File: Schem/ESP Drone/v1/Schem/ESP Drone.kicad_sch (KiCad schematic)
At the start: 80 parts, among them J1 Micro_SD_Card, J2 GEPRC M10 FPV, J3 Conn_01x03_Pin, J4 Conn_01x03_Pin, J5 Conn_01x03_Pin, J6 Conn_01x03_Pin, J7 Conn_Coaxial, U1 ESP32-S2-WROVER, U2 TPS563200, U3 MPU-6050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

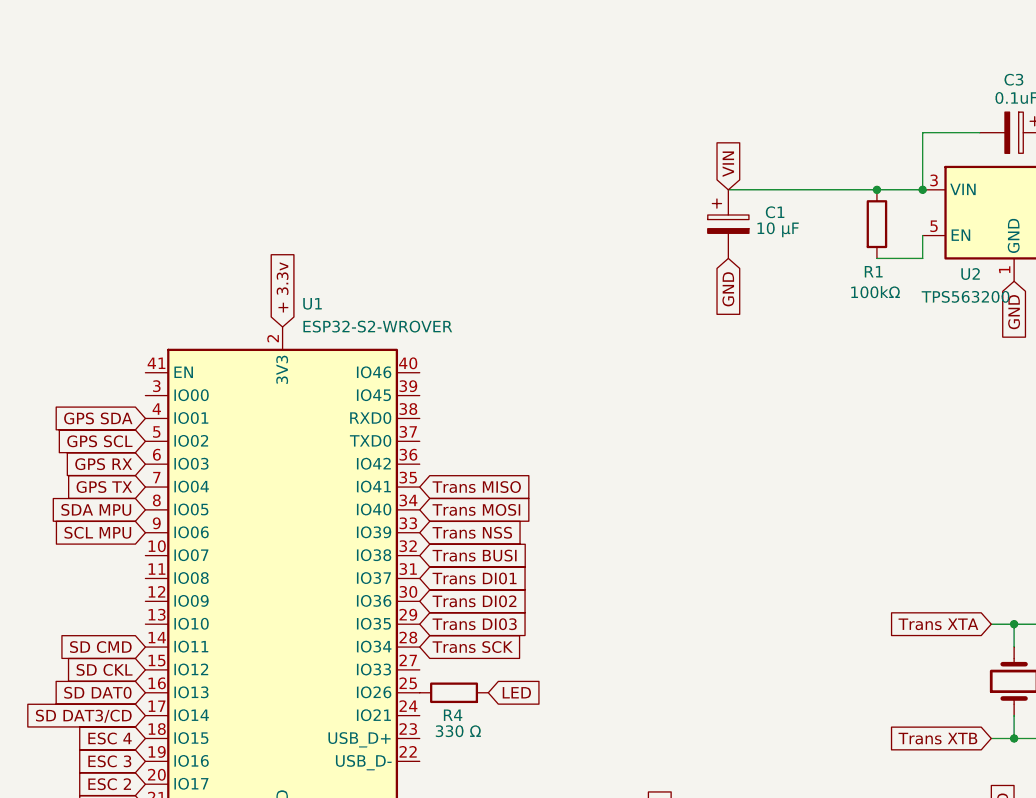
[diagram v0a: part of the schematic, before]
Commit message: feat: BMP280, LoRa-Protokoll, i18n, Blackbox, Pre-flight Check
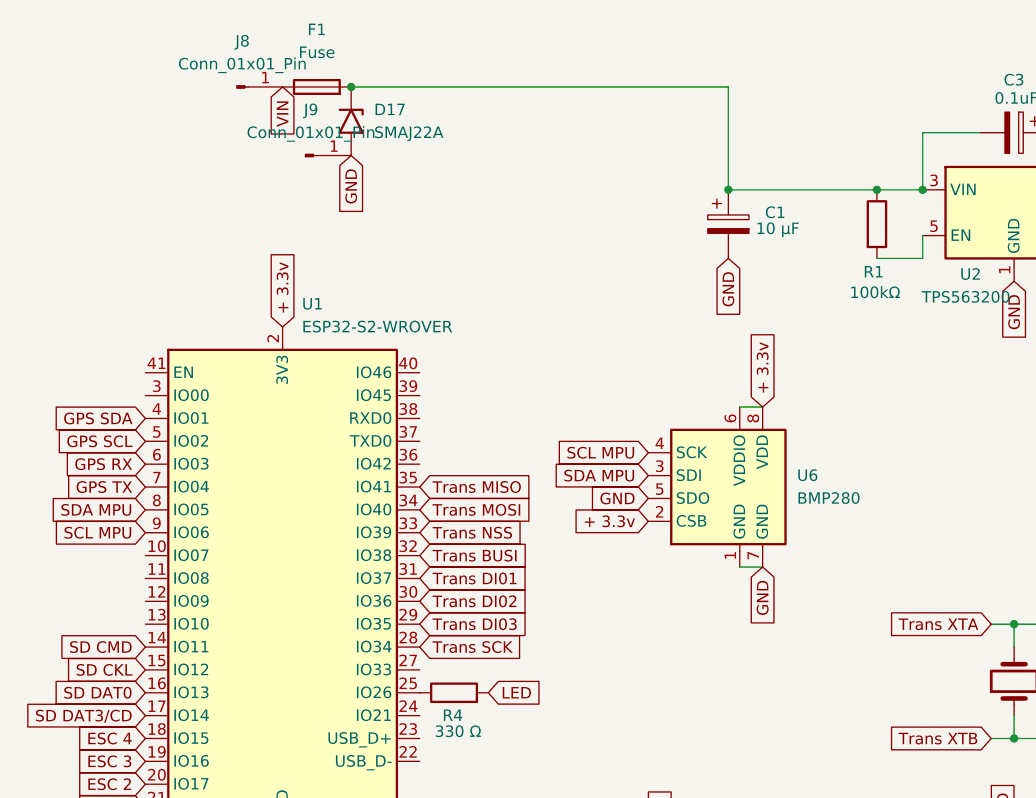
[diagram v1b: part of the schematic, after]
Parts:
- added D17: SMAJ22A, Diode_SMD:D_SMA, symbol Diode:SMAJ22A
- added F1: Fuse, Fuse:Fuseholder_Blade_Mini_Keystone_3568, symbol Device:Fuse
- added J8, J9: Conn_01x01_Pin, Library:high power throu hole, symbol Connector:Conn_01x01_Pin
- added U6: BMP280, Package_LGA:Bosch_LGA-8_2x2.5mm_P0.65mm_ClockwisePinNumbering, symbol Sensor_Pressure:BMP280
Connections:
- net + 3.3v: now also U6.2 (CSB), U6.6 (VDDIO), U6.8 (VDD)
- net GND: now also D17.2 (A2), J9.1 (Pin_1), U6.1 (GND), U6.5 (SDO), U6.7 (GND)
- net SCL MPU: now also U6.4 (SCK)
- net SDA MPU: now also U6.3 (SDI)
- net VIN: now also F1.1, J8.1 (Pin_1); no longer C1.1, C3.2, R1.1, U2.3 (VIN)
- new net: C1.1, C3.2, D17.1 (A1), F1.2, R1.1, U2.3 (VIN)
